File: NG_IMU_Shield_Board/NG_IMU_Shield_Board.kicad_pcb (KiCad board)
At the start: 2 copper layers, 87.6 x 45.7 mm, 21 parts, among them J1 Conn_01x04_Female, J2 Conn_01x02_Male, J3 Conn_01x10_Female, J4 Conn_01x03_Female, J6 Conn_01x11_Male, U1 SN75ALS175, U2 Level_Converter, U3 Teensy_v4.0

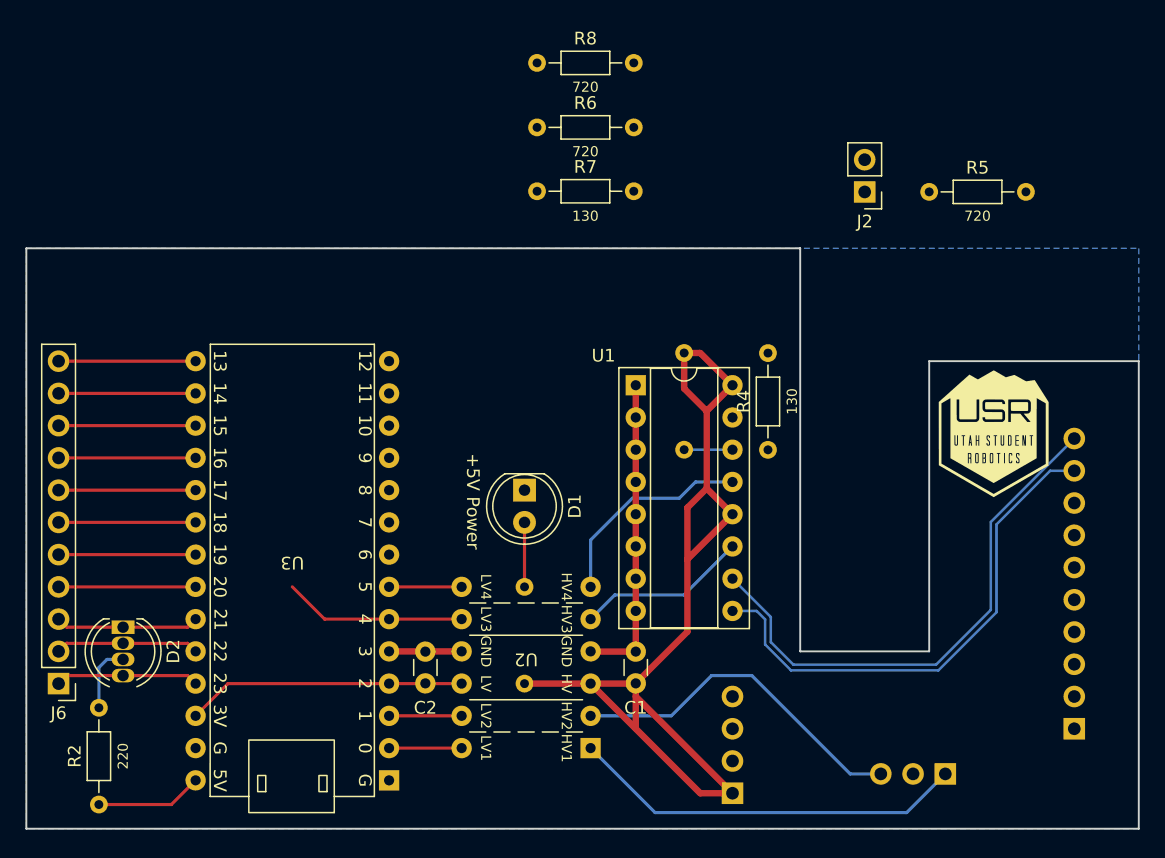
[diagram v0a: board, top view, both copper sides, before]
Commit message: Simplified and updated footprints to ease routing
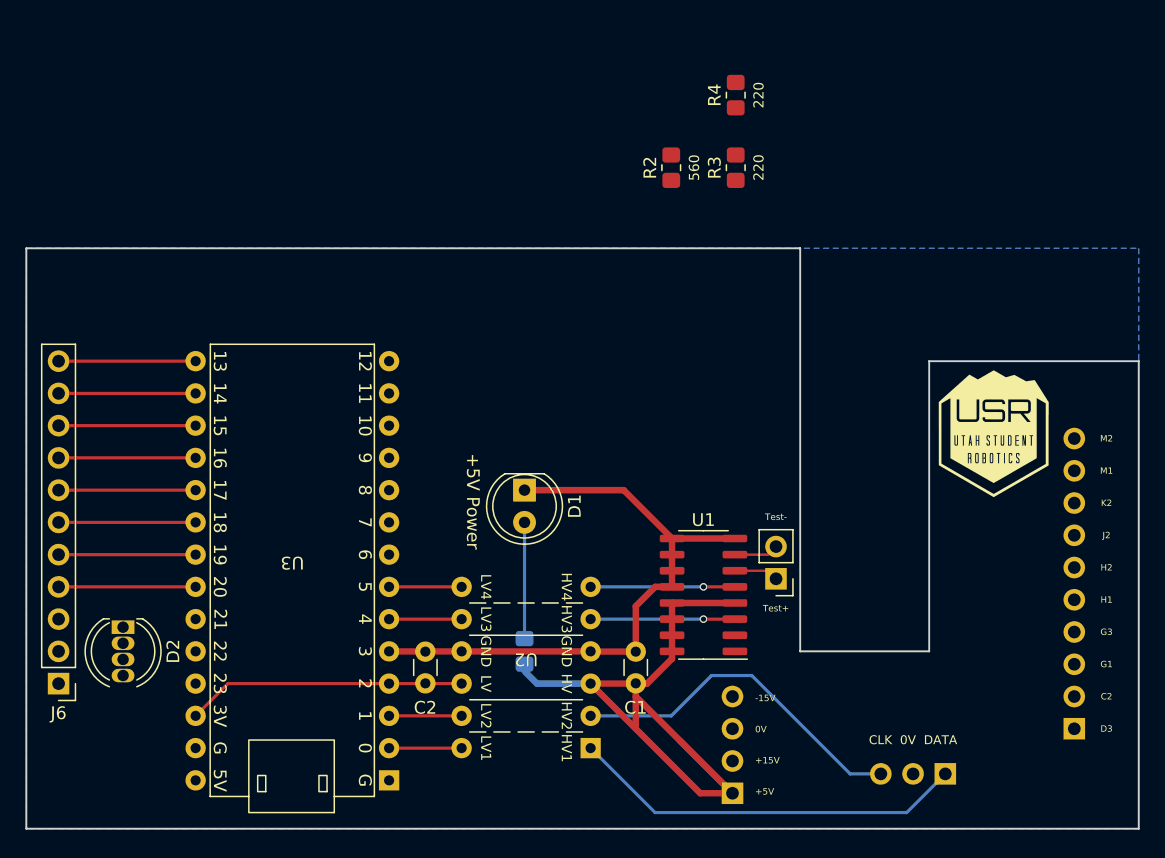
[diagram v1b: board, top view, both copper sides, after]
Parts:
- removed R5, R6, R8: 720, Resistor_THT:R_Axial_DIN0204_L3.6mm_D1.6mm_P7.62mm_Horizontal
- removed R7: 130, Resistor_THT:R_Axial_DIN0204_L3.6mm_D1.6mm_P7.62mm_Horizontal
- R1: footprint Resistor_THT:R_Axial_DIN0204_L3.6mm_D1.6mm_P7.62mm_Horizontal -> Resistor_SMD:R_0805_2012Metric_Pad1.20x1.40mm_HandSolder
- R2: value 220 -> 560; footprint Resistor_THT:R_Axial_DIN0204_L3.6mm_D1.6mm_P7.62mm_Horizontal -> Resistor_SMD:R_0805_2012Metric_Pad1.20x1.40mm_HandSolder
- R3: value 720 -> 220; footprint Resistor_THT:R_Axial_DIN0204_L3.6mm_D1.6mm_P7.62mm_Horizontal -> Resistor_SMD:R_0805_2012Metric_Pad1.20x1.40mm_HandSolder; moved to F.Cu
- R4: value 130 -> 220; footprint Resistor_THT:R_Axial_DIN0204_L3.6mm_D1.6mm_P7.62mm_Horizontal -> Resistor_SMD:R_0805_2012Metric_Pad1.20x1.40mm_HandSolder
- U1: value SN75ALS175 -> SN75LBC175; footprint Package_DIP:DIP-16_W7.62mm_Socket -> Package_SO:SOIC-16_3.9x9.9mm_P1.27mm
- moved R2 62.0 mm to (156.2, 52.1), turned to 90 degrees
- moved J2 31.3 mm to (164.5, 84.5)
- moved R4 28.1 mm to (161.3, 46.4)
- moved U1 17.4 mm to (158.8, 85.7), turned to 180 degrees
- moved R3 15.2 mm to (161.3, 52.1), turned to 90 degrees
- moved R1 5.08 mm to (144.7, 90.2)
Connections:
- D2 pad 1: /RLED -> Net-(D2-Pad1)
- D2 pad 2: /BLED -> Net-(D2-Pad2)
- D2 pad 3: Net-(D2-Pad3) -> /3V3
- D2 pad 4: /GLED -> Net-(D2-Pad4)
- R2 pad 1: Net-(D2-Pad3) -> Net-(D2-Pad1)
- R2 pad 2: Net-(R2-Pad2) -> /RLED
- R3 pad 1: /+5V -> Net-(D2-Pad4)
- R3 pad 2: /Test+ -> /GLED
- R4 pad 1: /Test+ -> Net-(D2-Pad2)
- R4 pad 2: /Test- -> /BLED
- U1 pad 1: /0V -> /Ready-
- U1 pad 10: /Ready+ -> /0V
- U1 pad 11: /Ready_clean -> /0V
- U1 pad 12: /+5V -> /0V
- U1 pad 13: /Test_clean -> /+5V
- U1 pad 14: /Test+ -> /+5V
- U1 pad 15: /Test- -> /+5V
- U1 pad 2: /0V -> /Ready+
- U1 pad 3: /0V -> /Ready_clean
- U1 pad 4: /0V -> /+5V
- U1 pad 5: /0V -> /Test_clean
- U1 pad 6: /0V -> /Test+
- U1 pad 7: /0V -> /Test-
- U1 pad 9: /Ready- -> /0V
- U3 pad 28: Net-(R2-Pad2) -> unconnected-(U3-Pad28)
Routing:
- net /Ready+: track 42.3 -> 0.00 mm
- net /Ready-: track 40.6 -> 0.00 mm
- net /+5V: track 82.6 -> 57.1 mm
- net /0V: track 30.2 -> 48.4 mm
- net /RLED: track 11.3 -> 0.00 mm
- net /BLED: track 11.3 -> 0.00 mm
- net /GLED: track 10.4 -> 0.00 mm
- net /Ready_in: track 14.4 -> 5.71 mm
- net Net-(R2-Pad2): track 8.41 -> 0.00 mm
- net /Test_clean: track 16.8 -> 11.4 mm, vias 0 -> 1
- net Net-(D2-Pad3): track 5.34 -> 0.00 mm
- net Net-(D1-Pad2): track 5.08 -> 8.61 mm
- net /Test-: track 0.00 -> 3.50 mm
- net /Ready_clean: track 13.5 -> 11.4 mm, vias 0 -> 1
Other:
- board text added: "560"
- board text added: "Test+"
- board text added: "Test-"
- board text removed: "130"
- board text removed: "720"

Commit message: Finished routing board
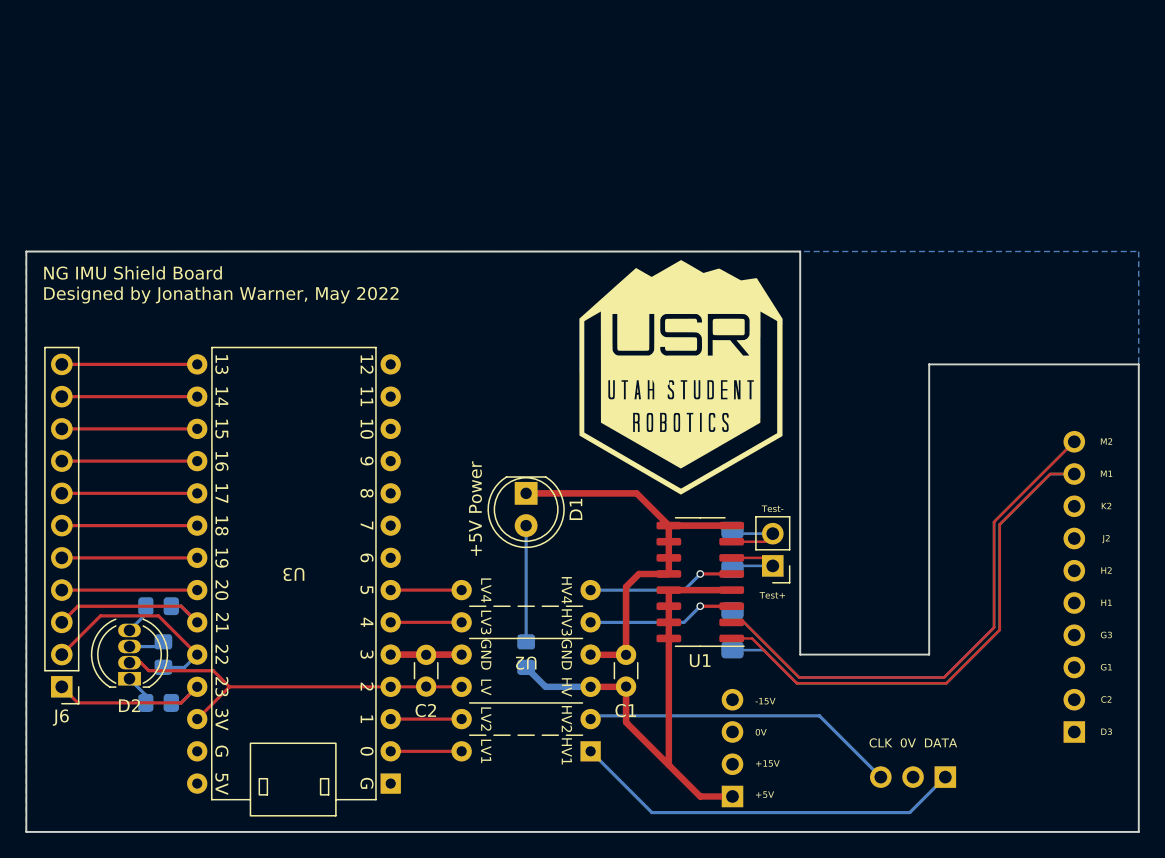
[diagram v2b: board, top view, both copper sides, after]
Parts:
- removed the G*** at (181.6, 73.0)
- added G***: LOGO, NG_IMU_footprints:USR_medium, F.Cu at (157.0, 68.6)
- added R5: 120, Resistor_SMD:R_1206_3216Metric_Pad1.30x1.75mm_HandSolder, B.Cu at (161.0, 88.5)
- added R6: 120, Resistor_SMD:R_1206_3216Metric_Pad1.30x1.75mm_HandSolder, B.Cu at (161.0, 82.2)
- D2: value LED_RBAG -> LED_GABR
- R2, R3, R4: moved to B.Cu
- moved R4 63.0 mm to (116.2, 90.4), turned to -90 degrees
- moved R3 62.0 mm to (115.8, 94.2), turned to 0 degrees
- moved R2 53.1 mm to (115.8, 86.6), turned to 0 degrees
- moved D2 4.10 mm to (113.5, 92.3), turned to 90 degrees
- moved J2 1.05 mm to (164.2, 83.4)
- moved U1 1.05 mm to (158.5, 84.7)
- moved C1 0.80 mm to (152.7, 92.9)
- moved J6 0.36 mm to (108.2, 93.0)
- moved D1 0.28 mm to (144.8, 77.7)
- moved U3 0.28 mm to (134.1, 100.6)
- moved R1 0.28 mm to (144.8, 90.4)
- moved C2 0.26 mm to (136.9, 92.9)
- moved U2 0.25 mm to (144.8, 91.7)
- moved J1 0.25 mm to (161.0, 101.6)
- moved J3 0.25 mm to (188.0, 96.5)
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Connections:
- D2 pad 2: Net-(D2-Pad2) -> /3V3
- D2 pad 3: /3V3 -> Net-(D2-Pad3)
- R2 pad 1: Net-(D2-Pad1) -> Net-(D2-Pad4)
- R3 pad 1: Net-(D2-Pad4) -> Net-(D2-Pad1)
- R4 pad 1: Net-(D2-Pad2) -> Net-(D2-Pad3)
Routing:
- net /Ready+: track 0.00 -> 83.0 mm
- net /Ready-: track 0.00 -> 79.9 mm
- net /+5V: track 57.1 -> 40.6 mm
- net /BLED: track 0.00 -> 16.3 mm
- net /RLED: track 0.00 -> 14.3 mm
- net /GLED: track 0.00 -> 14.3 mm
- net /0V: track 48.4 -> 38.6 mm
- net /3V3: track 22.0 -> 30.5 mm
- net /Test-: track 3.50 -> 6.39 mm
- net /CLK_clean: track 27.4 -> 24.6 mm
- net Net-(D2-Pad4): track 0.00 -> 2.44 mm
- net Net-(D2-Pad1): track 0.00 -> 2.44 mm
- net Net-(D2-Pad3): track 0.00 -> 2.30 mm
- net /Test+: track 3.50 -> 5.50 mm
- net Net-(D1-Pad2): track 8.61 -> 9.16 mm
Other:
- board text added: "120"

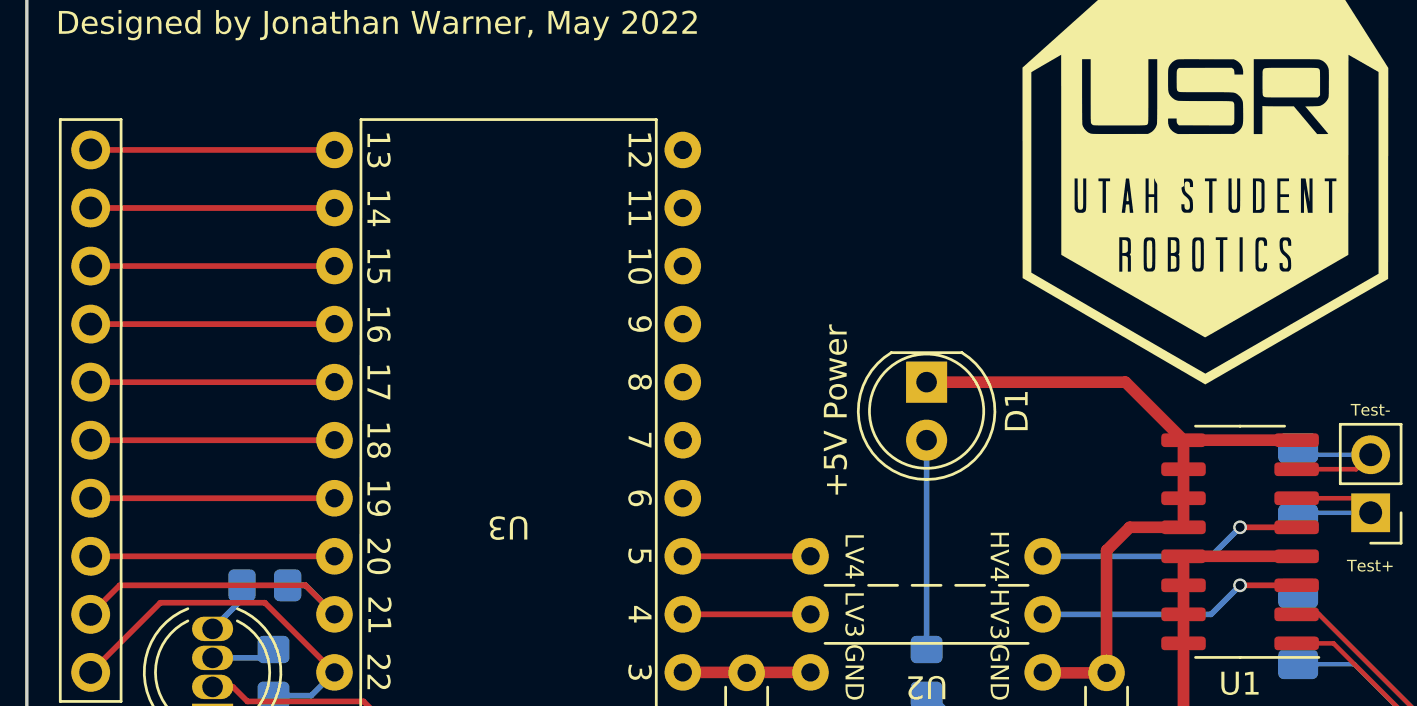
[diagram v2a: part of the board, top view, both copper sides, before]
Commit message: Added signal names, level shifter sockets, and small fix
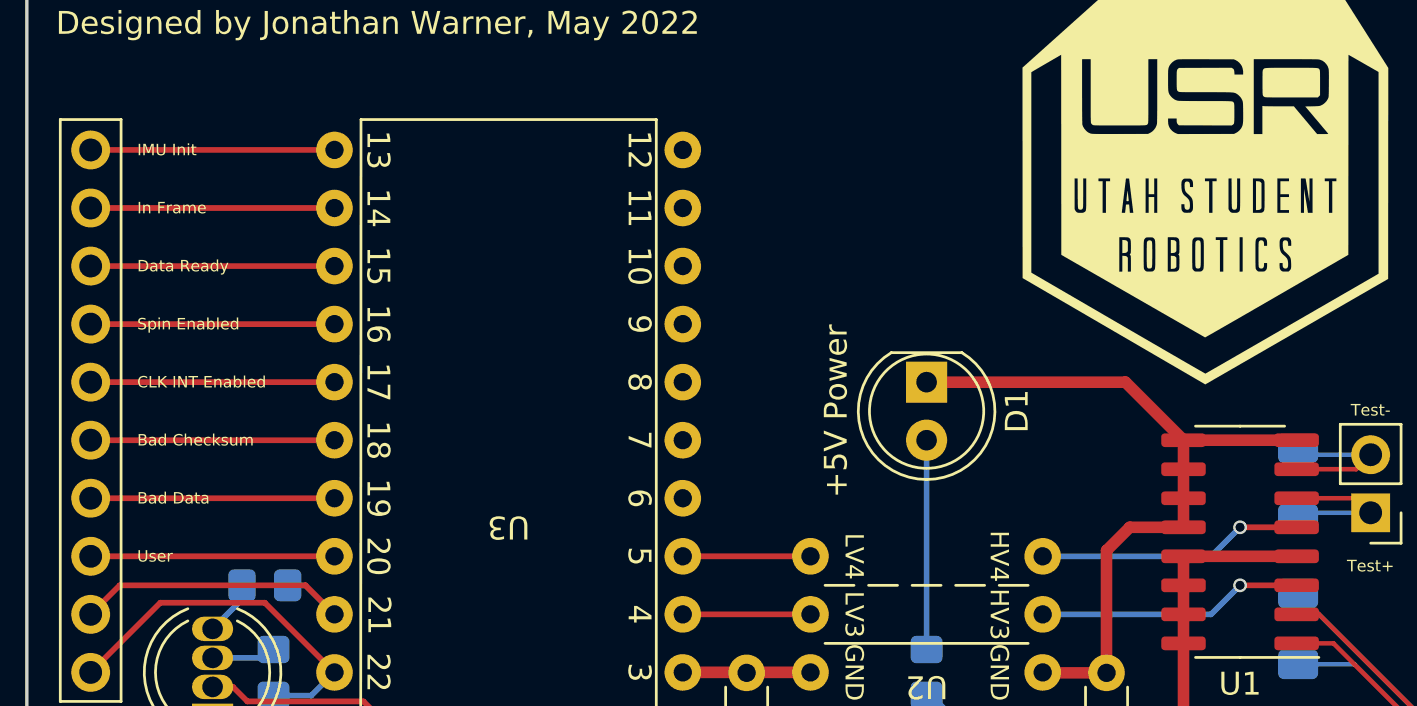
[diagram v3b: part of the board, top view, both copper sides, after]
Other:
- board text added: "Bad Checksum"
- board text added: "Bad Data"
- board text added: "Blue"
- board text added: "CLK INT Enabled"
- board text added: "Data Ready"
- board text added: "Green"
- board text added: "IMU Init"
- board text added: "In Frame"
- board text added: "Red"
- board text added: "Spin Enabled"
- board text added: "User"

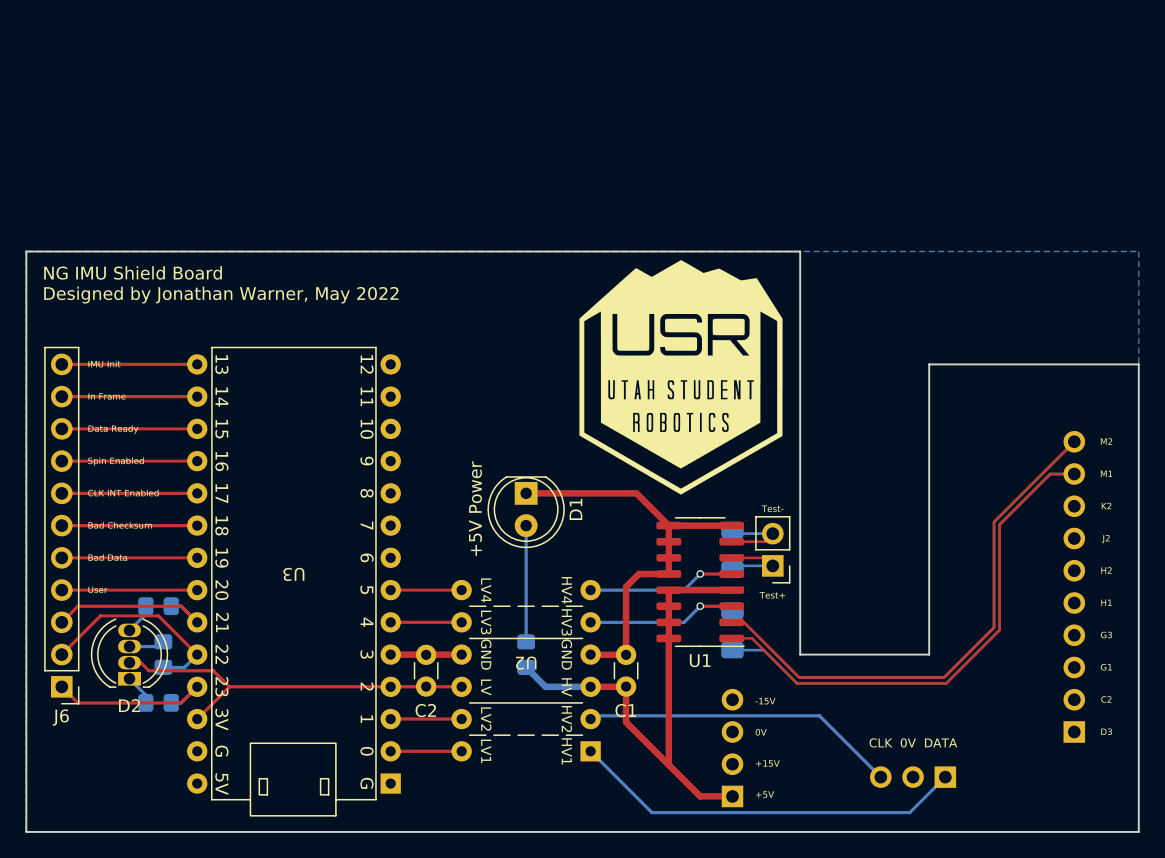
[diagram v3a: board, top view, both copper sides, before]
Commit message: Moved status LED, added more user signals, other improvements
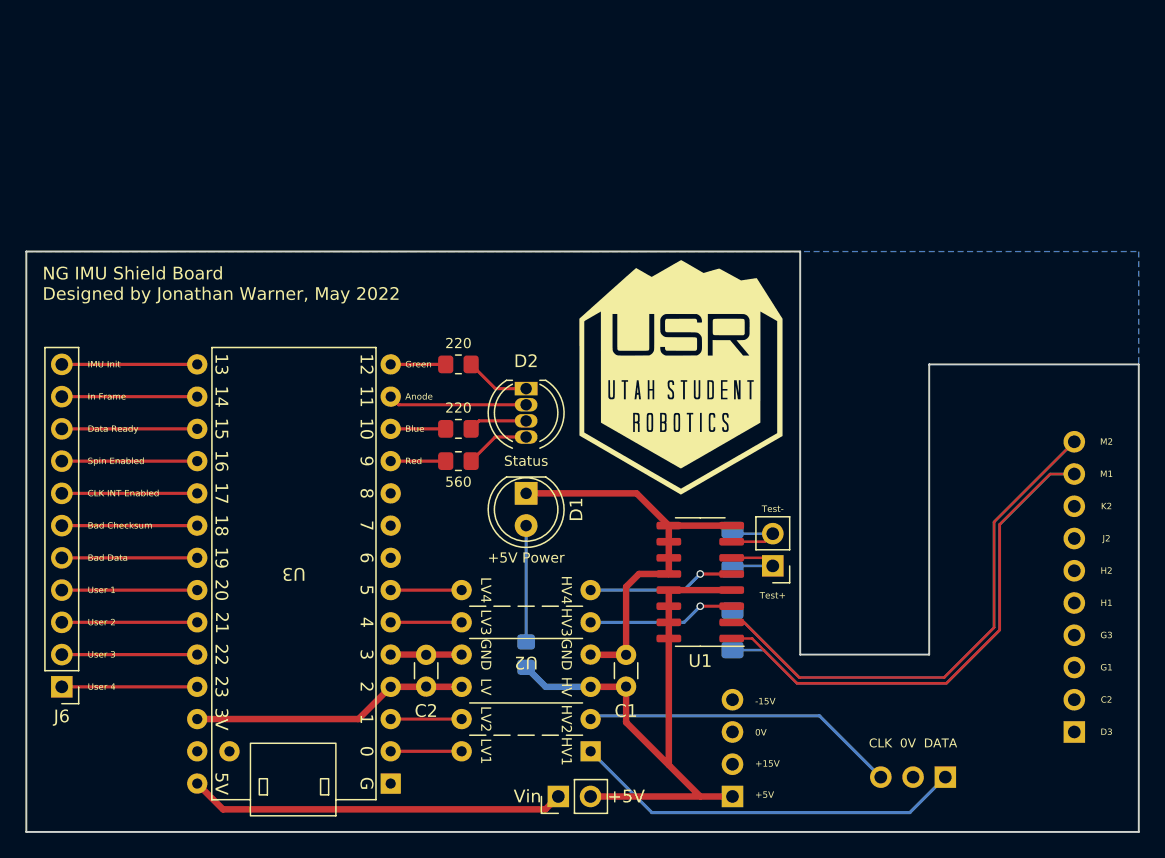
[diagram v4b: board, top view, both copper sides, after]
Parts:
- added JP1: Jumper_2_Open, Connector_PinHeader_2.54mm:PinHeader_1x02_P2.54mm_Vertical, F.Cu at (147.3, 101.6)
- R2, R3, R4: moved to F.Cu
- moved D2 38.7 mm to (144.8, 69.5), turned to -90 degrees
- moved R3 35.6 mm to (139.4, 67.6), turned to 180 degrees
- moved R4 29.3 mm to (139.4, 72.6), turned to 180 degrees
- moved R2 26.2 mm to (139.4, 75.2), turned to 180 degrees
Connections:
- net /user renamed /user1
- D2 pad 2: /3V3 -> /ALED
- J6 pad 1: /GLED -> /user4
- J6 pad 2: /BLED -> /user3
- J6 pad 3: /RLED -> /user2
- U3 pad 11: unconnected-(U3-Pad11) -> /RLED
- U3 pad 12: unconnected-(U3-Pad12) -> /BLED
- U3 pad 13: unconnected-(U3-Pad13) -> /ALED
- U3 pad 14: unconnected-(U3-Pad14) -> /GLED
- U3 pad 23: /RLED -> /user2
- U3 pad 24: /BLED -> /user3
- U3 pad 25: /GLED -> /user4
- U3 pad 28: unconnected-(U3-Pad28) -> /Vin
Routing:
- net /Vin: track 0.00 -> 29.7 mm
- net /BLED: track 16.3 -> 4.33 mm
- net /ALED: track 0.00 -> 10.9 mm
- net /user4: track 0.00 -> 10.7 mm
- net /user3: track 0.00 -> 10.7 mm
- net /user2: track 0.00 -> 10.7 mm
- net /RLED: track 14.3 -> 4.33 mm
- net /GLED: track 14.3 -> 4.33 mm
- net /3V3: track 30.5 -> 21.9 mm
- net /+5V: track 40.6 -> 49.2 mm
- net Net-(D2-Pad1): track 2.44 -> 5.13 mm
- net Net-(D2-Pad4): track 2.44 -> 5.12 mm
- net Net-(D2-Pad3): track 2.30 -> 4.59 mm
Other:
- board text added: "Anode"
- board text added: "User 1"
- board text added: "User 2"
- board text added: "User 3"
- board text added: "User 4"
- board text removed: "+5V Power"
- board text removed: "560"
- board text removed: "User"
